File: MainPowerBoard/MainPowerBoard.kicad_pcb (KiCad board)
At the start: 2 copper layers, 177.8 x 177.8 mm, 250 parts, among them J101 CONN_01X04, J102 CONN_01X04, J103 CONN_01X04, J104 CONN_01X02, J105 CONN_01X02, J106 CONN_01X06, J107 CONN_01X06, J108 CONN_01X04, J109 CONN_01X04, J110 CONN_01X02, J111 CONN_01X02, J112 CONN_01X02, J113 CONN_01X02, J114 CONN_01X02, J115 CONN_01X02, J116 CONN_01X02, J117 CONN_01X02, J118 CONN_01X02, J119 CONN_01X02, J120 CONN_01X02, J121 CONN_01X02, J122 CONN_01X02, J123 CONN_01X02, J124 CONN_01X02, J125 CONN_01X02, J126 CONN_01X02, J127 CONN_01X02, J128 CONN_01X02, J129 CONN_01X02, J130 MOUNTING_HOLE, J131 MOUNTING_HOLE, J132 MOUNTING_HOLE, J133 MOUNTING_HOLE, SW701 KS-01Q-01, U1001 LMR16030S, U1101 LMR16030S, U1201 LMR16030S, U1301 LMR16030S, U1401 LMR16030S, U201 LMR16030S, U301 LMR16030S, U701 AP2204RA-5.0TRG1, U702 TLV271IDBVR, U703 LTC2950-1, U704 TLC393, U801 LMR16030S, U901 LMR16030S

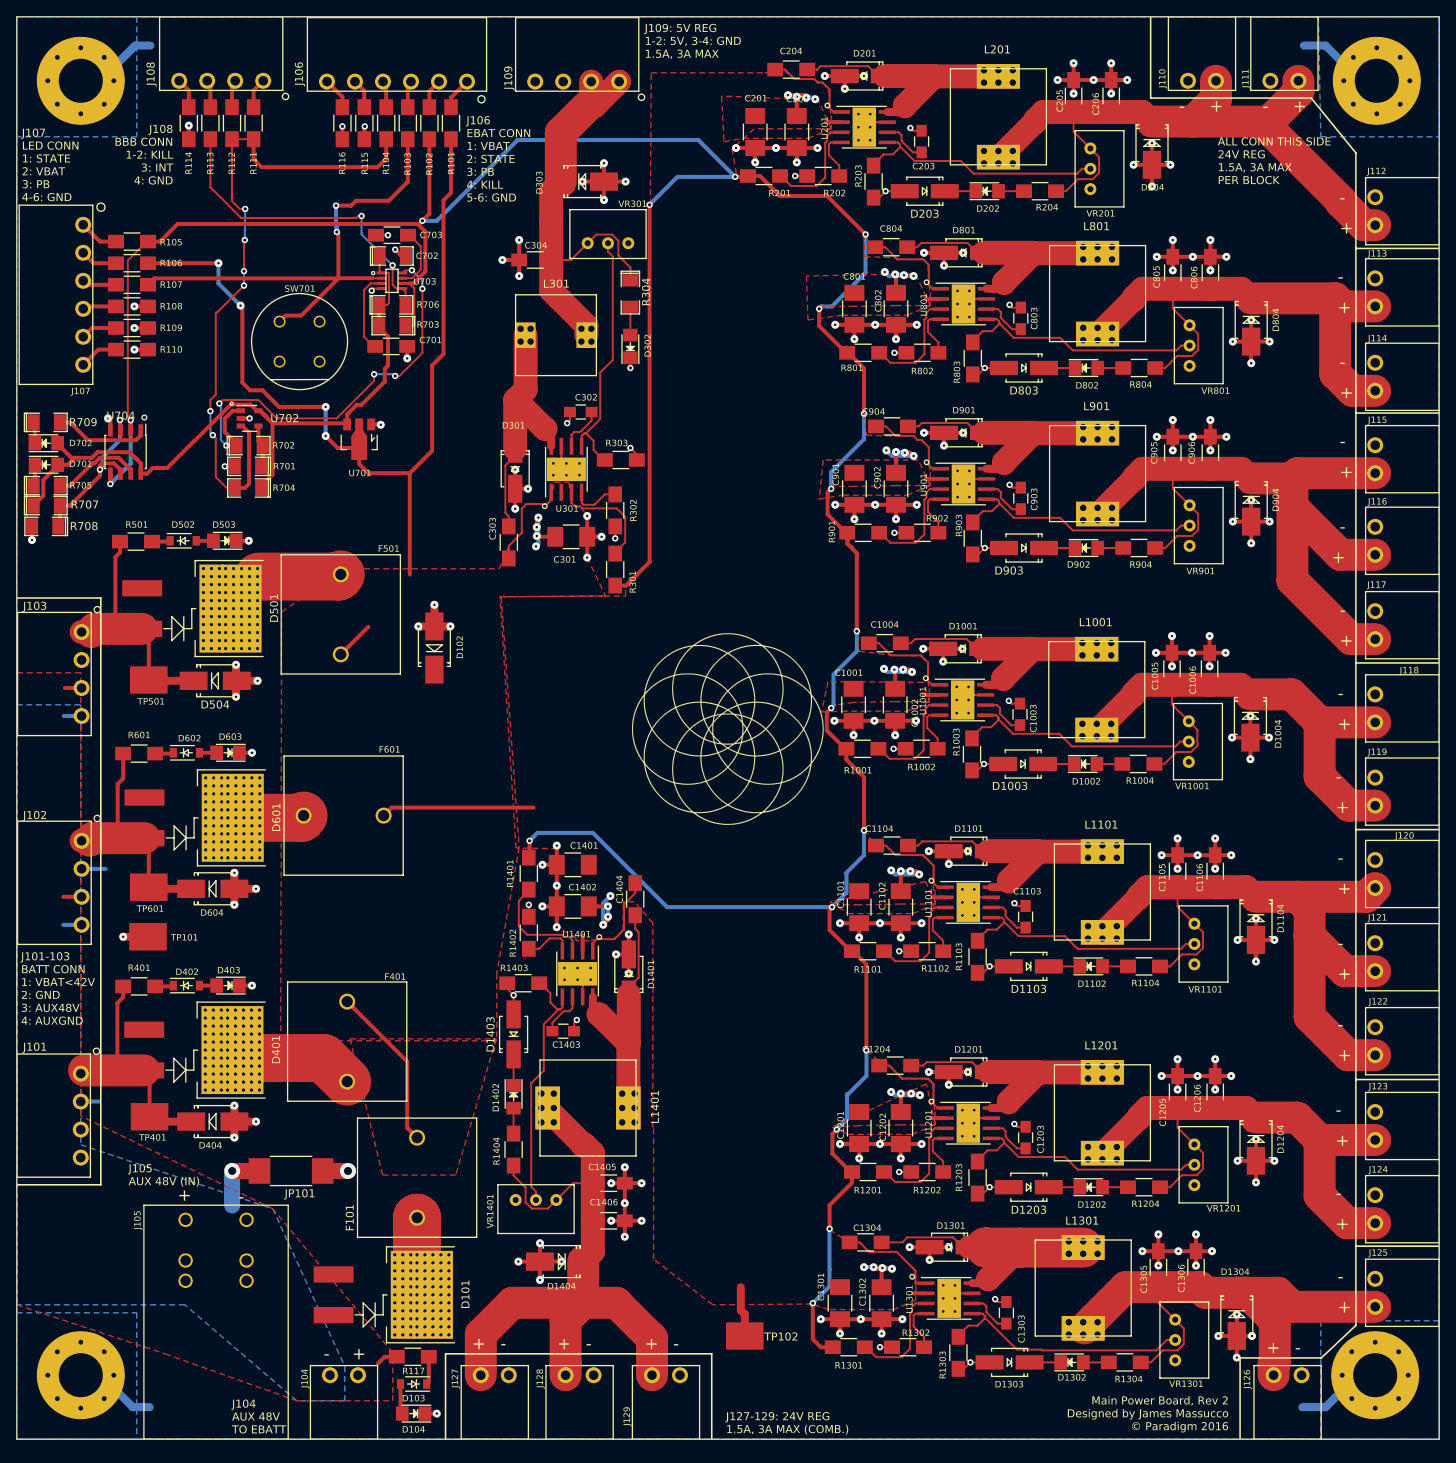
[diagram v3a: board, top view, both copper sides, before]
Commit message: Updated MPB Power Selector Circuit Schematic and added it to the PCB
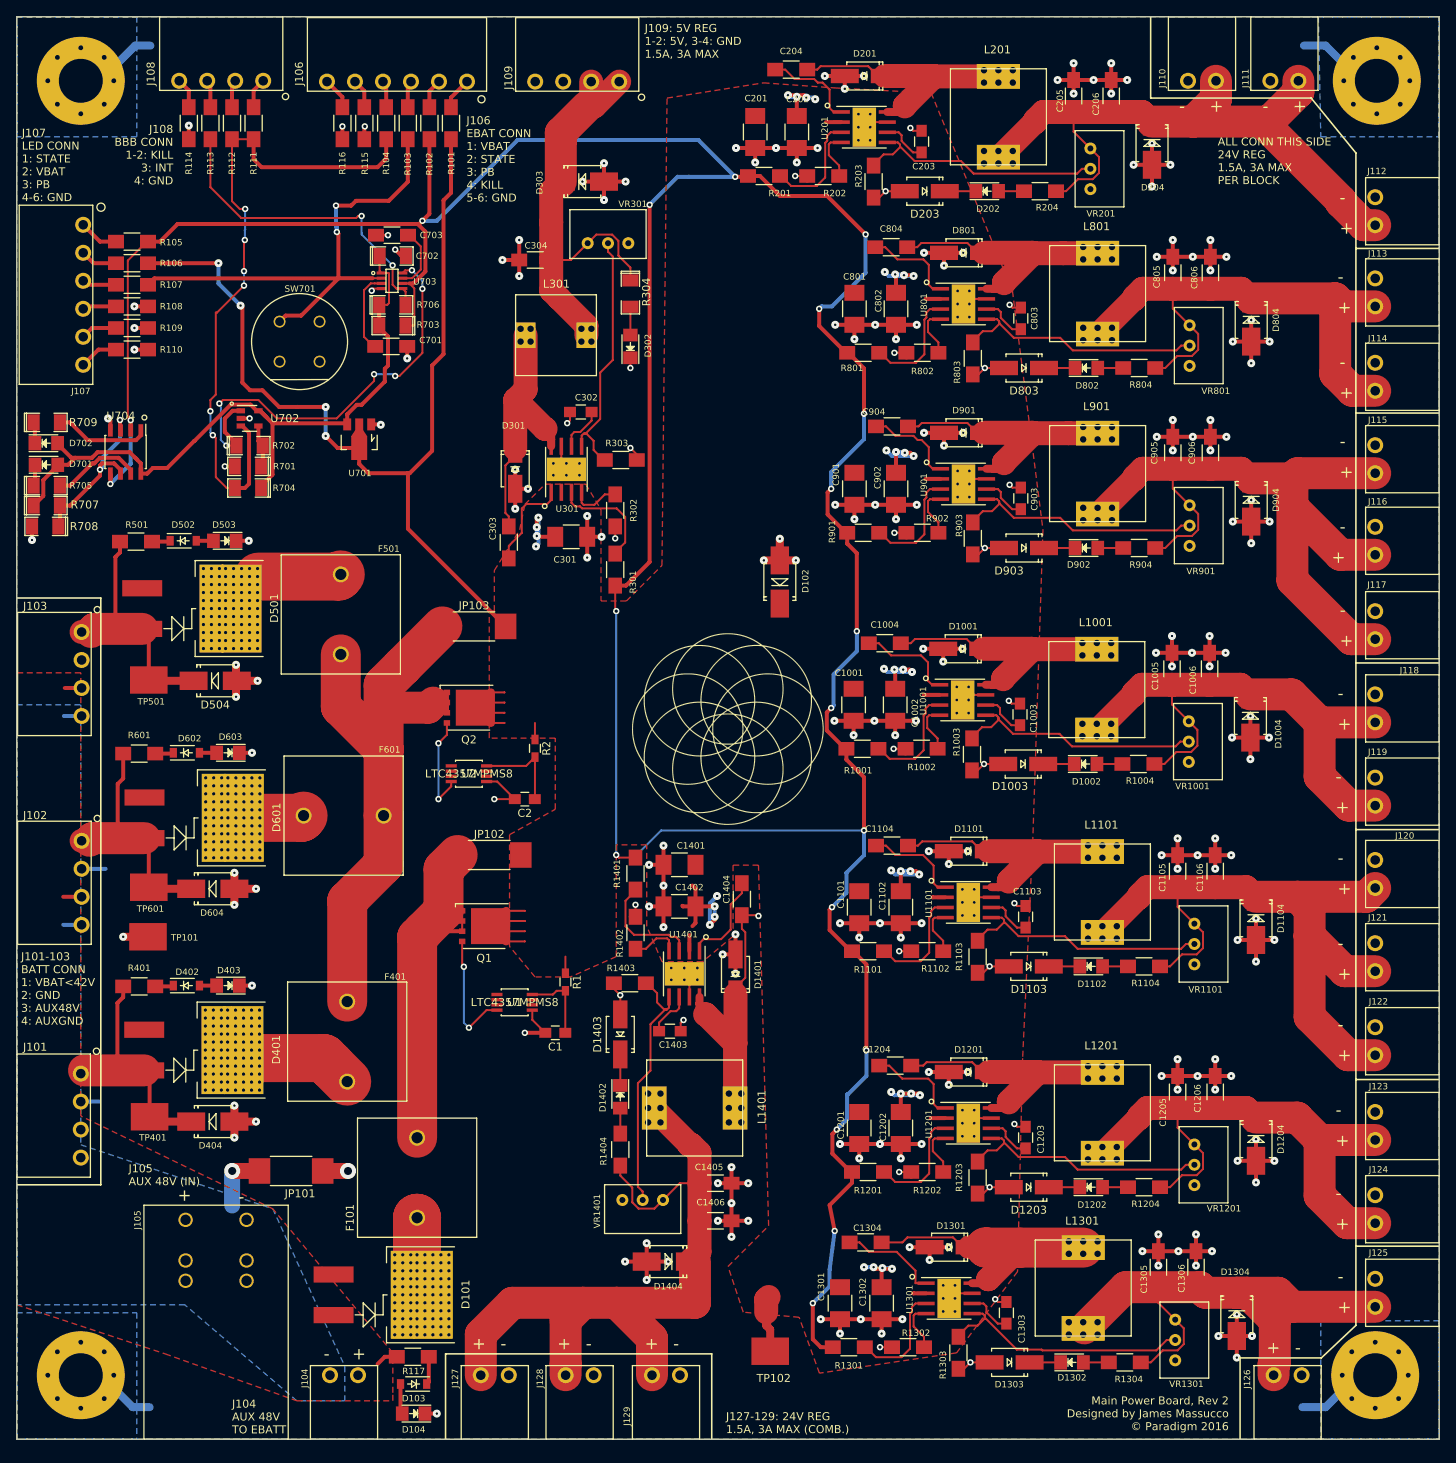
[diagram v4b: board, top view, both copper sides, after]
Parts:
- removed the G*** at (88.9, 88.9)
- added C1: 1u, Capacitors_SMD:C_0805_HandSoldering, F.Cu at (67.3, 127.0)
- added C2: 1u, Capacitors_SMD:C_0805_HandSoldering, F.Cu at (63.5, 97.8)
- added JP102: JUMPER, Resistors_SMD:R_2512_HandSoldering, F.Cu at (59.1, 104.8)
- added JP103: JUMPER, Resistors_SMD:R_2512_HandSoldering, F.Cu at (57.1, 76.2)
- added Q1: CSD19502Q5B, TO_SOT_Packages_SMD:TDSON-8-1, F.Cu at (58.4, 113.7)
- added Q2: CSD19502Q5B, TO_SOT_Packages_SMD:TDSON-8-1, F.Cu at (56.5, 86.4)
- added R1: 100, Resistors_SMD:R_0603_HandSoldering, F.Cu at (68.6, 120.7)
- added R2: 100, Resistors_SMD:R_0603_HandSoldering, F.Cu at (64.8, 91.4)
- added U1: LTC4357MPMS8, hyperCustom:LTC4357MPMS8, F.Cu at (62.2, 123.2)
- added U2: LTC4357MPMS8, hyperCustom:LTC4357MPMS8, F.Cu at (56.5, 94.6)
- moved D102 44.0 mm to (95.4, 70.6)
- moved C1403 13.3 mm to (81.6, 126.8)
- moved C1404 13.3 mm to (90.6, 110.3)
- moved D1404 13.3 mm to (81.4, 155.6)
- moved R1403 13.3 mm to (76.6, 120.8)
- moved U1401 13.3 mm to (83.4, 119.6)
- moved D1402 13.3 mm to (75.4, 135.0)
- moved D1403 13.3 mm to (75.4, 127.2)
- moved R1404 13.3 mm to (75.4, 141.6)
- moved VR1401 13.3 mm to (73.5, 152.1)
- moved C1401 13.3 mm to (82.8, 106.0)
- moved C1402 13.3 mm to (82.8, 111.2)
- moved C1405 13.3 mm to (87.3, 145.8)
- moved C1406 13.3 mm to (87.3, 150.5)
- moved D1401 13.3 mm to (89.8, 119.7)
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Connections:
- net /5V0_REG renamed /5V0_REG1
- C1001 pad 1: /VCC_BATT_COMB -> /MAIN_POWER
- C1002 pad 1: /VCC_BATT_COMB -> /MAIN_POWER
- C1101 pad 1: /VCC_BATT_COMB -> /MAIN_POWER
- C1102 pad 1: /VCC_BATT_COMB -> /MAIN_POWER
- C1201 pad 1: /VCC_BATT_COMB -> /MAIN_POWER
- C1202 pad 1: /VCC_BATT_COMB -> /MAIN_POWER
- C1301 pad 1: /VCC_BATT_COMB -> /MAIN_POWER
- C1302 pad 1: /VCC_BATT_COMB -> /MAIN_POWER
- C1401 pad 1: /VCC_BATT_COMB -> /MAIN_POWER
- C1402 pad 1: /VCC_BATT_COMB -> /MAIN_POWER
- C1405 pad 1: /24V0_REG8 -> /5 Volt Regulator -- 2/24V0_REG
- C1406 pad 1: /24V0_REG8 -> /5 Volt Regulator -- 2/24V0_REG
- C201 pad 1: /VCC_BATT_COMB -> /MAIN_POWER
- C202 pad 1: /VCC_BATT_COMB -> /MAIN_POWER
- C301 pad 1: /VCC_BATT_COMB -> /MAIN_POWER
- C801 pad 1: /VCC_BATT_COMB -> /MAIN_POWER
- C802 pad 1: /VCC_BATT_COMB -> /MAIN_POWER
- C901 pad 1: /VCC_BATT_COMB -> /MAIN_POWER
- C902 pad 1: /VCC_BATT_COMB -> /MAIN_POWER
- D101 pad 1: /48V0_FROM_LINE -> /48V0_FROM_LINE_UNPROT
- D102 pad 1: /VCC_BATT_COMB -> /MAIN_POWER
- D1404 pad 1: /24V0_REG8 -> /5 Volt Regulator -- 2/24V0_REG
- F101 pad 2: /VCC_BATT_COMB -> /48V0_FROM_LINE
- F401 pad 2: /VCC_BATT_COMB -> GND
- F501 pad 2: /VCC_BATT_COMB -> GND
- F601 pad 2: /VCC_BATT_COMB -> GND
- J101 pad 3: /48V0_FROM_LINE -> /48V0_FROM_LINE_UNPROT
- J102 pad 3: /48V0_FROM_LINE -> /48V0_FROM_LINE_UNPROT
- J103 pad 3: /48V0_FROM_LINE -> /48V0_FROM_LINE_UNPROT
- J104 pad 2: /48V0_FROM_LINE -> /48V0_FROM_LINE_UNPROT
- J105 pad 1: /48V0_FROM_LINE -> /48V0_FROM_LINE_UNPROT
- J127 pad 1: /24V0_REG8 -> /5V0_REG2
- J128 pad 1: /24V0_REG8 -> /5V0_REG2
- J129 pad 1: /24V0_REG8 -> /5V0_REG2
- L1401 pad 2: /24V0_REG8 -> /5 Volt Regulator -- 2/24V0_REG
- R101 pad 1: /VCC_BATT_COMB -> /MAIN_POWER
- R106 pad 1: /VCC_BATT_COMB -> /MAIN_POWER
- R117 pad 1: /48V0_FROM_LINE -> /48V0_FROM_LINE_UNPROT
- R1404 pad 1: /24V0_REG8 -> /5 Volt Regulator -- 2/24V0_REG
- TP102 pad ~: /VCC_BATT_COMB -> /MAIN_POWER
- U1001 pad 2: /VCC_BATT_COMB -> /MAIN_POWER
- U1101 pad 2: /VCC_BATT_COMB -> /MAIN_POWER
- U1201 pad 2: /VCC_BATT_COMB -> /MAIN_POWER
- U1301 pad 2: /VCC_BATT_COMB -> /MAIN_POWER
- U1401 pad 2: /VCC_BATT_COMB -> /MAIN_POWER
- U201 pad 2: /VCC_BATT_COMB -> /MAIN_POWER
- U301 pad 2: /VCC_BATT_COMB -> /MAIN_POWER
- U701 pad VI: /VCC_BATT_COMB -> /MAIN_POWER
- U801 pad 2: /VCC_BATT_COMB -> /MAIN_POWER
- U901 pad 2: /VCC_BATT_COMB -> /MAIN_POWER
- VR1001 pad 1: (no net) -> Net-(VR1001-Pad1)
- VR1101 pad 1: (no net) -> Net-(VR1101-Pad1)
- VR1201 pad 1: (no net) -> Net-(VR1201-Pad1)
- VR1301 pad 1: (no net) -> Net-(VR1301-Pad1)
- VR1401 pad 1: (no net) -> Net-(VR1401-Pad1)
- VR1401 pad 3: /24V0_REG8 -> /5 Volt Regulator -- 2/24V0_REG
- VR201 pad 1: (no net) -> Net-(VR201-Pad1)
- VR301 pad 1: (no net) -> Net-(VR301-Pad1)
- VR801 pad 1: (no net) -> Net-(VR801-Pad1)
- VR901 pad 1: (no net) -> Net-(VR901-Pad1)
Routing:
- net /MAIN_POWER: track 0.00 -> 268.4 mm, vias 0 -> 40
- net /VCC_BATT_COMB: track 258.8 -> 0.00 mm, vias 40 -> 0
- net GND: track 609.5 -> 698.8 mm, vias 226 -> 228
- net /24V0_REG8: track 87.2 -> 0.00 mm
- net /5V0_REG2: track 0.00 -> 54.4 mm
- net /5 Volt Regulator -- 2/24V0_REG: track 0.00 -> 44.2 mm
- net /48V0_FROM_LINE: track 7.17 -> 44.9 mm
- net /STATE: track 435.5 -> 457.5 mm, vias 18 -> 19
- net Net-(Q1-Pad4): track 0.00 -> 15.6 mm, vias 0 -> 2
- net Net-(C1404-Pad2): track 32.5 -> 47.4 mm, vias 0 -> 1
- net Net-(Q2-Pad4): track 0.00 -> 12.8 mm, vias 0 -> 2
- net Net-(C204-Pad2): track 32.3 -> 45.0 mm
- net Net-(C1304-Pad2): track 33.8 -> 46.5 mm
- net Net-(C1204-Pad2): track 32.3 -> 45.0 mm
- net Net-(C1104-Pad2): track 32.8 -> 45.5 mm
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- added copper zone on F.Cu, net /48V0_FROM_LINE_UNPROT
- added copper zone on F.Cu, net /MAIN_POWER
- removed copper zone on F.Cu, net /48V0_FROM_LINE
- removed copper zone on F.Cu, net /VCC_BATT_COMB
